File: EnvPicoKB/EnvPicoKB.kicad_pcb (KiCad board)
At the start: 2 copper layers, 21.5 x 51.3 mm, 46 parts, among them J1 Conn_01x04, J2 SKRKAEE020, J3 2.54mm header 01x20, J4 2.54mm header 01x20, J5 Conn_01x03_Male, U1 TLV75533PDBVR, U3 RP2040, Y1 3225_4P

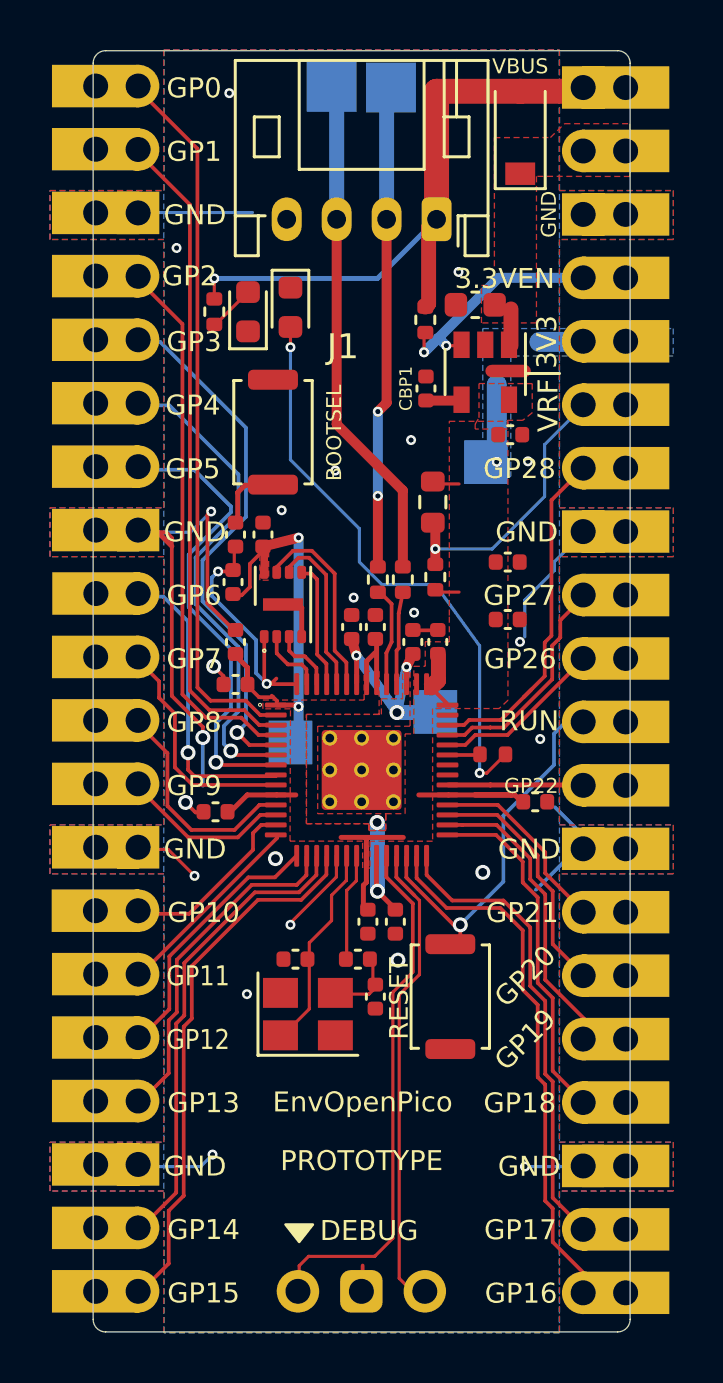
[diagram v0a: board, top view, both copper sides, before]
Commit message: woops, wrong JST connector lol.
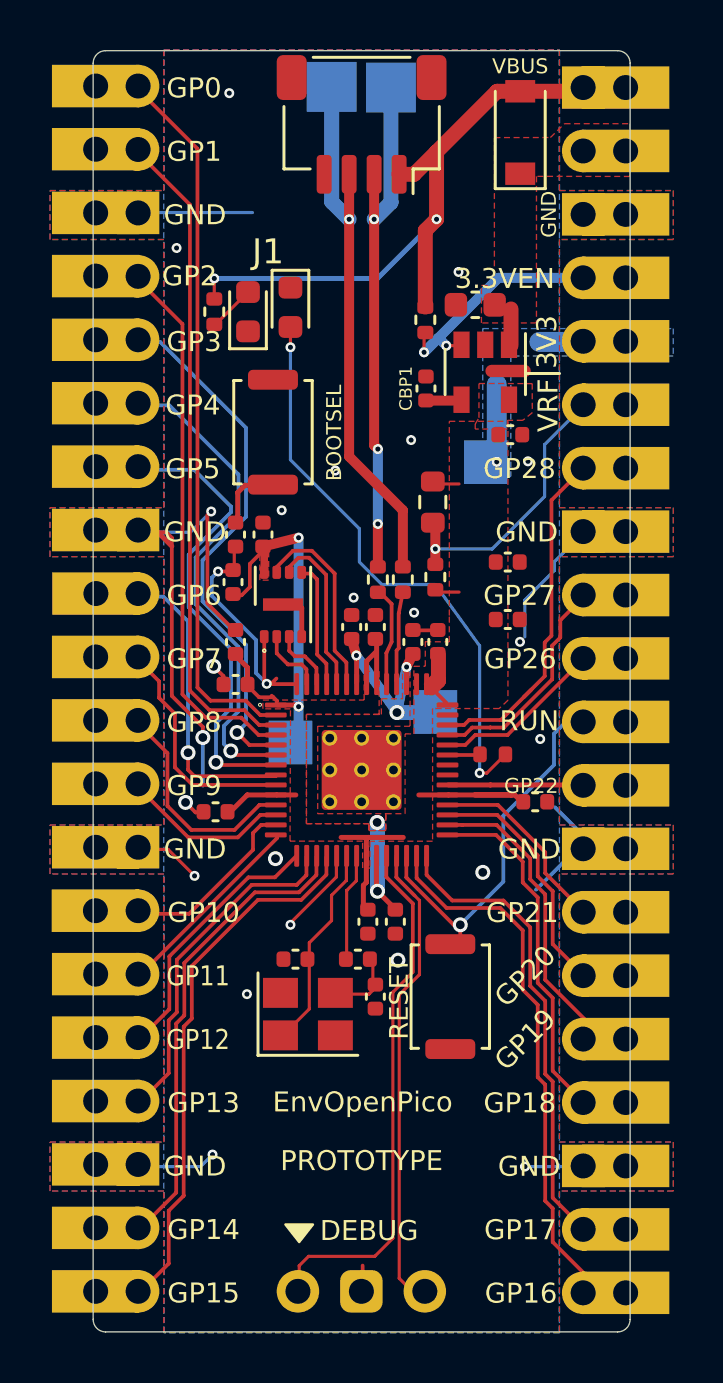
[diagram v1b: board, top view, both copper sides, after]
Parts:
- J1: footprint Connector_JST:JST_PH_S4B-PH-K_1x04_P2.00mm_Horizontal -> Connector_JST:JST_SH_SM04B-SRSS-TB_1x04-1MP_P1.00mm_Horizontal
- moved J1 4.84 mm to (103.7, 60.2)
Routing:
- net USB_D+: track 19.4 -> 21.3 mm, vias 2 -> 3
- net USB_D-: track 20.4 -> 22.2 mm, vias 0 -> 1
- net VBUS: track 28.4 -> 29.4 mm, vias 1 -> 2
